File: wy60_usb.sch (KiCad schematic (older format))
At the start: 220 parts, among them J1 AVR-ISP-6, U1 ATmega32A-PU

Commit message: fix annotation
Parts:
- renumbered D110 to D100, D111 to D101, D112 to D102, D113 to D103, D12 to D11, D13 to D12, D14 to D13, D15 to D14, D16 to D15, D17 to D16, D18 to D17, D19 to D18, D20 to D19, D21 to D20, D22 to D21, D23 to D22, D24 to D23, D25 to D24, D26 to D25, D27 to D26, D28 to D27, D29 to D28, D30 to D29, D31 to D30, D32 to D31, D33 to D32, D34 to D33, D35 to D34, D36 to D35, D37 to D36, D38 to D37, D39 to D38, D40 to D39, D41 to D40, D42 to D41, D43 to D42, D44 to D43, D45 to D44, D46 to D45, D47 to D46, D48 to D47, D49 to D48, D50 to D49, D51 to D50, D52 to D51, D53 to D52, D54 to D53, D55 to D54, D56 to D55, D57 to D56, D58 to D57, D59 to D58, D60 to D59, D61 to D60, D62 to D61, D63 to D62, D64 to D63, D65 to D64, D66 to D65, D67 to D66, D68 to D67, D69 to D68, D70 to D69, D71 to D70, D72 to D71, D74 to D72, D75 to D73, D76 to D74, D77 to D75, D78 to D76, D79 to D77, D80 to D78, D81 to D79, D82 to D80, D83 to D81, D84 to D82, D85 to D83, D86 to D84, D87 to D85, D88 to D86, D89 to D87, D90 to D88, D91 to D89, D92 to D90, D93 to D91, D94 to D92, D95 to D93, D96 to D94, D97 to D95, D98 to D96, D104 to D97, D108 to D98, D109 to D99, MX11 to MX10, MX110 to MX100, MX111 to MX101, MX12 to MX11, MX13 to MX12, MX14 to MX13, MX15 to MX14, MX16 to MX15, MX17 to MX16, MX18 to MX17, MX19 to MX18, MX20 to MX19, MX21 to MX20, MX22 to MX21, MX23 to MX22, MX24 to MX23, MX25 to MX24, MX26 to MX25, MX27 to MX26, MX28 to MX27, MX29 to MX28, MX30 to MX29, MX31 to MX30, MX32 to MX31, MX33 to MX32, MX34 to MX33, MX35 to MX34, MX36 to MX35, MX37 to MX36, MX38 to MX37, MX39 to MX38, MX40 to MX39, MX41 to MX40, MX42 to MX41, MX43 to MX42, MX44 to MX43, MX45 to MX44, MX46 to MX45, MX47 to MX46, MX48 to MX47, MX49 to MX48, MX50 to MX49, MX51 to MX50, MX52 to MX51, MX53 to MX52, MX54 to MX53, MX55 to MX54, MX56 to MX55, MX57 to MX56, MX58 to MX57, MX59 to MX58, MX60 to MX59, MX61 to MX60, MX62 to MX61, MX63 to MX62, MX64 to MX63, MX65 to MX64, MX66 to MX65, MX67 to MX66, MX68 to MX67, MX69 to MX68, MX70 to MX69, MX72 to MX70, MX73 to MX71, MX74 to MX72, MX75 to MX73, MX76 to MX74, MX77 to MX75, MX78 to MX76, MX79 to MX77, MX80 to MX78, MX81 to MX79, MX82 to MX80, MX83 to MX81, MX84 to MX82, MX85 to MX83, MX86 to MX84, MX87 to MX85, MX88 to MX86, MX89 to MX87, MX90 to MX88, MX91 to MX89, MX10 to MX9, MX92 to MX90, MX93 to MX91, MX94 to MX92, MX95 to MX93, MX96 to MX94, MX102 to MX95, MX106 to MX96, MX107 to MX97, MX108 to MX98, MX109 to MX99

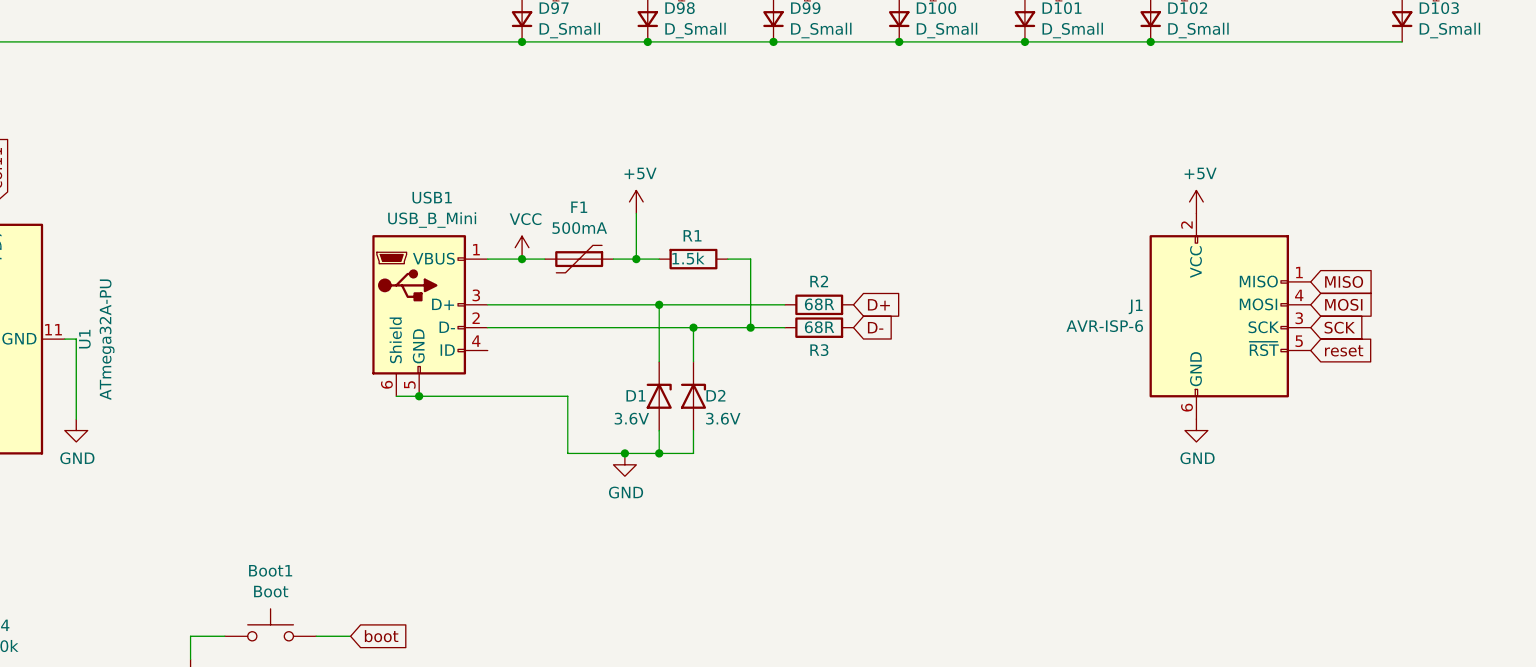
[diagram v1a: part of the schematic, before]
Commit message: added JST port for fixed cable
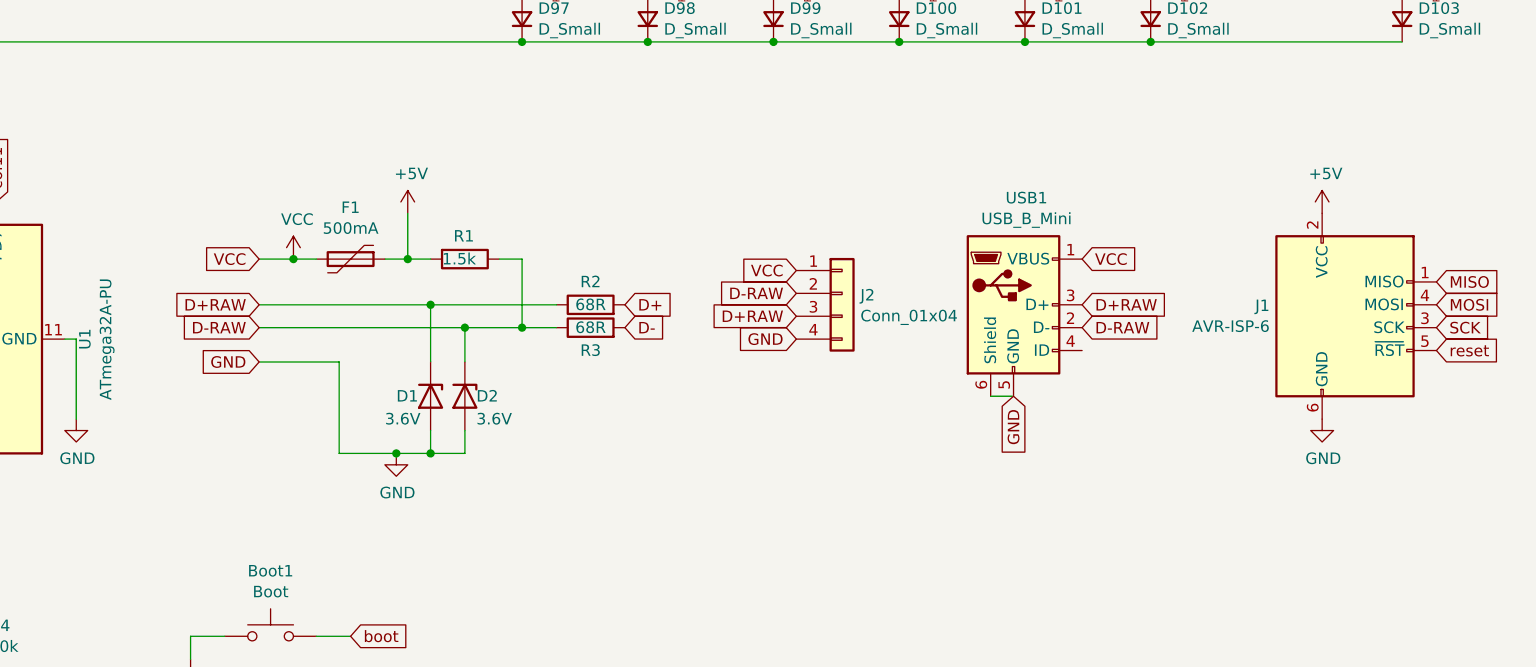
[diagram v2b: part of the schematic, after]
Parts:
- added J2: Conn_01x04, Connector_JST:JST_PH_S4B-PH-K_1x04_P2.00mm_Horizontal, symbol Connector_Generic:Conn_01x04
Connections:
- net GND: now also J2.4 (Pin_4)
- net VCC: now also J2.1 (Pin_1)
- net D-RAW: now reaches D2.1 (K), R1.1, R3.1, USB1.2 (D-)
- net D-RAW: now also J2.2 (Pin_2)
- net D+RAW: now reaches D1.1 (K), R2.1, USB1.3 (D+)
- net D+RAW: now also J2.3 (Pin_3)
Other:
- moved on the sheet: D1, D2, F1, J1, R1, R2, R3, USB1
